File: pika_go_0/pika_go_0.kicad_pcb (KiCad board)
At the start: 4 copper layers, 50 x 110 mm, 110 parts, among them J1 BAT, J2 MCU_DEBUG, J3 Micro_SD_Card_Det1, J4 Conn_01x02, J5 LCD, J6 USB_C_Receptacle_USB2.0_16P, J7 MIC, J8 SPK, Q1 BSS138, SW1 PWR, SW2 LSN, SW3 PTT, SW4 UP, SW5 DOWN, SW6 LEFT, SW7 RIGHT, U1 TPS610333DRLR, U10 MAX4467EKA_T, U2 BQ25895RTW, U3 MCP1703Ax-330xxMB, U4 STM32H733VGTx, U5 USB3300-EZK, U6 MCP1703Ax-500xxTT, U7 E22-900M30S, U8 CAM-M8Q-0, U9 SSM2305RMZ-REEL7, Y1 SG-210STF 24.0000ML0

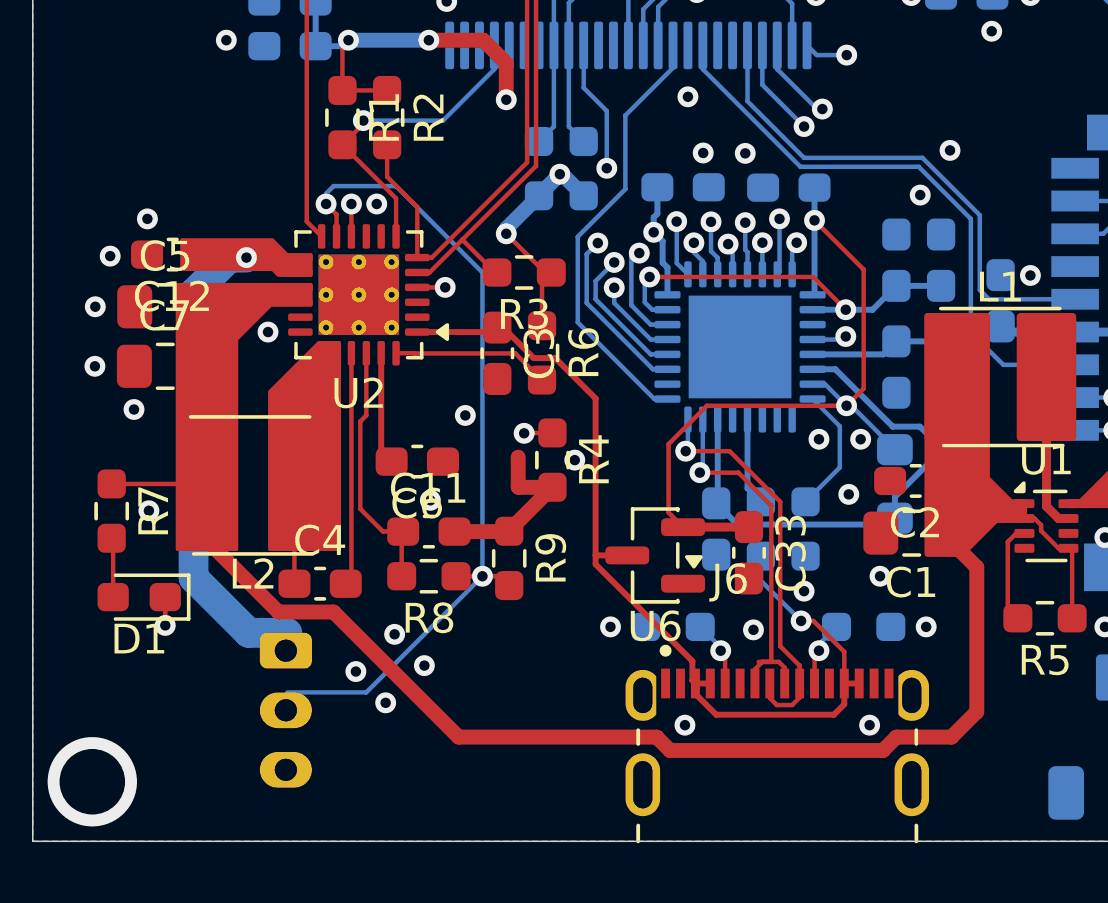
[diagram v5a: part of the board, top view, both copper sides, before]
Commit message: PCB changes, USB-C connector moved to back side
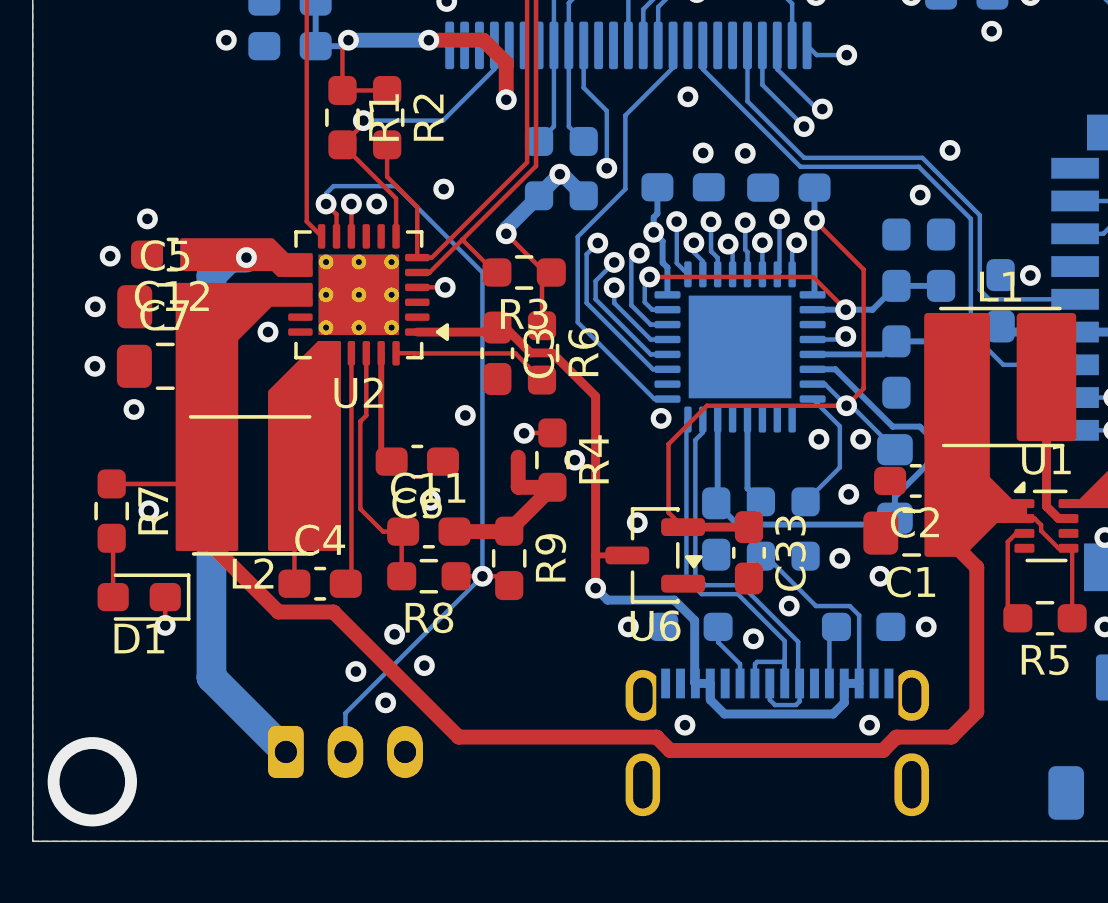
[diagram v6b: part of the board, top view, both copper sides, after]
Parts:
- J6: moved to B.Cu
- moved R19 6.40 mm to (57.9, 135.8), turned to 180 degrees
- moved R20 5.80 mm to (52.1, 135.8), turned to 0 degrees
- moved J1 3.40 mm to (38.5, 140.0), turned to 0 degrees
- turned J6 to 180 degrees
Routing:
- net /Power/BAT: track 15.7 -> 18.5 mm
- net USB_VBUS: track 32.2 -> 33.9 mm
- net /USB/USB_DP: track 12.5 -> 13.4 mm, vias 1 -> 0
- net Net-(J6-CC1): track 2.31 -> 2.00 mm, vias 1 -> 0
- net /USB/USB_DM: track 13.5 -> 13.3 mm, vias 1 -> 0
- net Net-(J6-CC2): vias 1 -> 0
- net GND: vias 157 -> 161

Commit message: Side and top buttons moved
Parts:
- moved SW3 10.0 mm to (31.6, 77.0)
- moved SW2 5.00 mm to (31.6, 55.0)
- moved SW1 3.00 mm to (55.0, 34.6)
- moved J8 0.67 mm to (59.0, 41.4), turned to 90 degrees
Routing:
- net /MCU/BTN_PTT: track 43.0 -> 34.3 mm
- net /MCU/BTN_LSN: track 59.9 -> 56.2 mm
- net Net-(J8-Pin_2): track 23.9 -> 26.3 mm
- net BTN_PWR: track 102.4 -> 103.6 mm
